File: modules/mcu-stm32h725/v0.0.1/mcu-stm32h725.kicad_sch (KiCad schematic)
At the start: 14 parts, among them J1 USB-C, U1 USB6B1RL, U2 TPS2116DRLR, U3 TLV62569DBVR

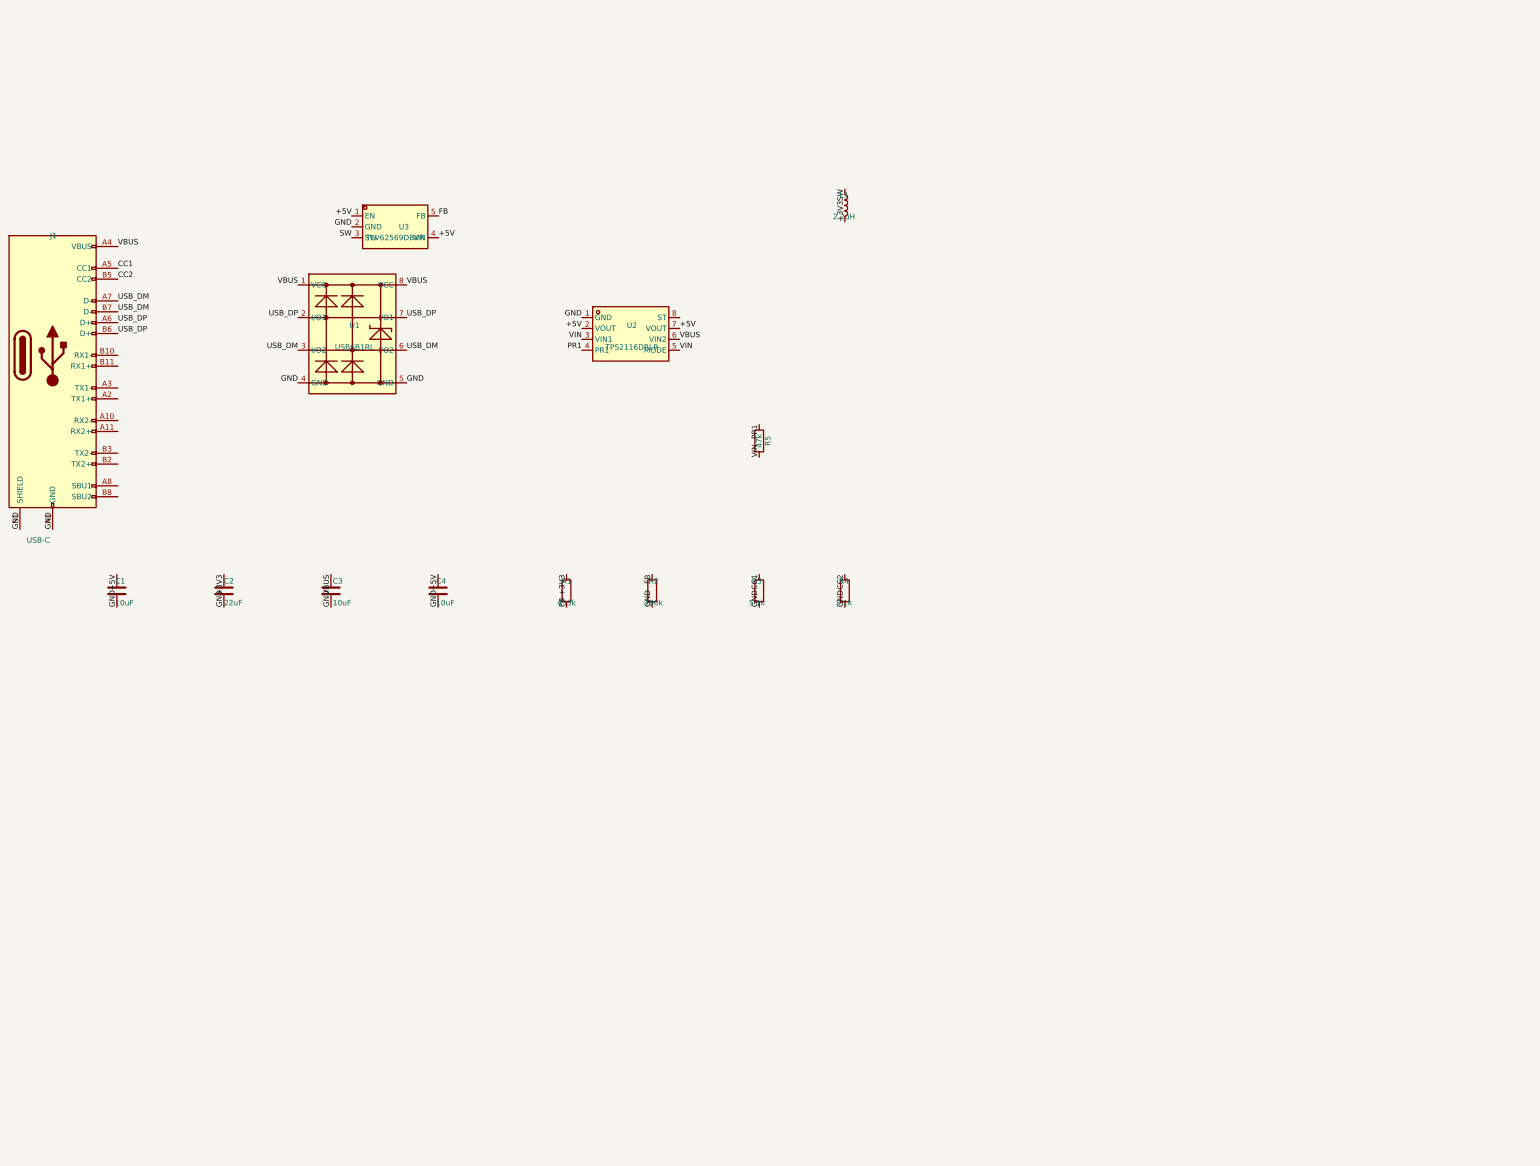
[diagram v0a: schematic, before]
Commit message: Complete mcu-stm32h725 schematic: MCU core + full GPIO breakout (ERC 0 errors)
Direct-SMPS power tree (VDDSMPS/VLXSMPS+L2/VFBSMPS=VCORE per DS13311 Table 16), full VDD/VCAP/VDDA decoupling, HSE crystal, BOOT0/NRST, USB to PA11/12. All 44 GPIO broken out by RAW pin name (no aliasing) to edge connectors J2 (Side A) + J3 (Side B). PWR_FLAGs + no-connects on unused USB-C SS/SBU + TPS2116 ST. 4-layer PCB chosen. ERC: 0 errors, 130 benign easyeda-symbol warnings.

Co-Authored-By: Claude Opus 4.8 <noreply@anthropic.com>
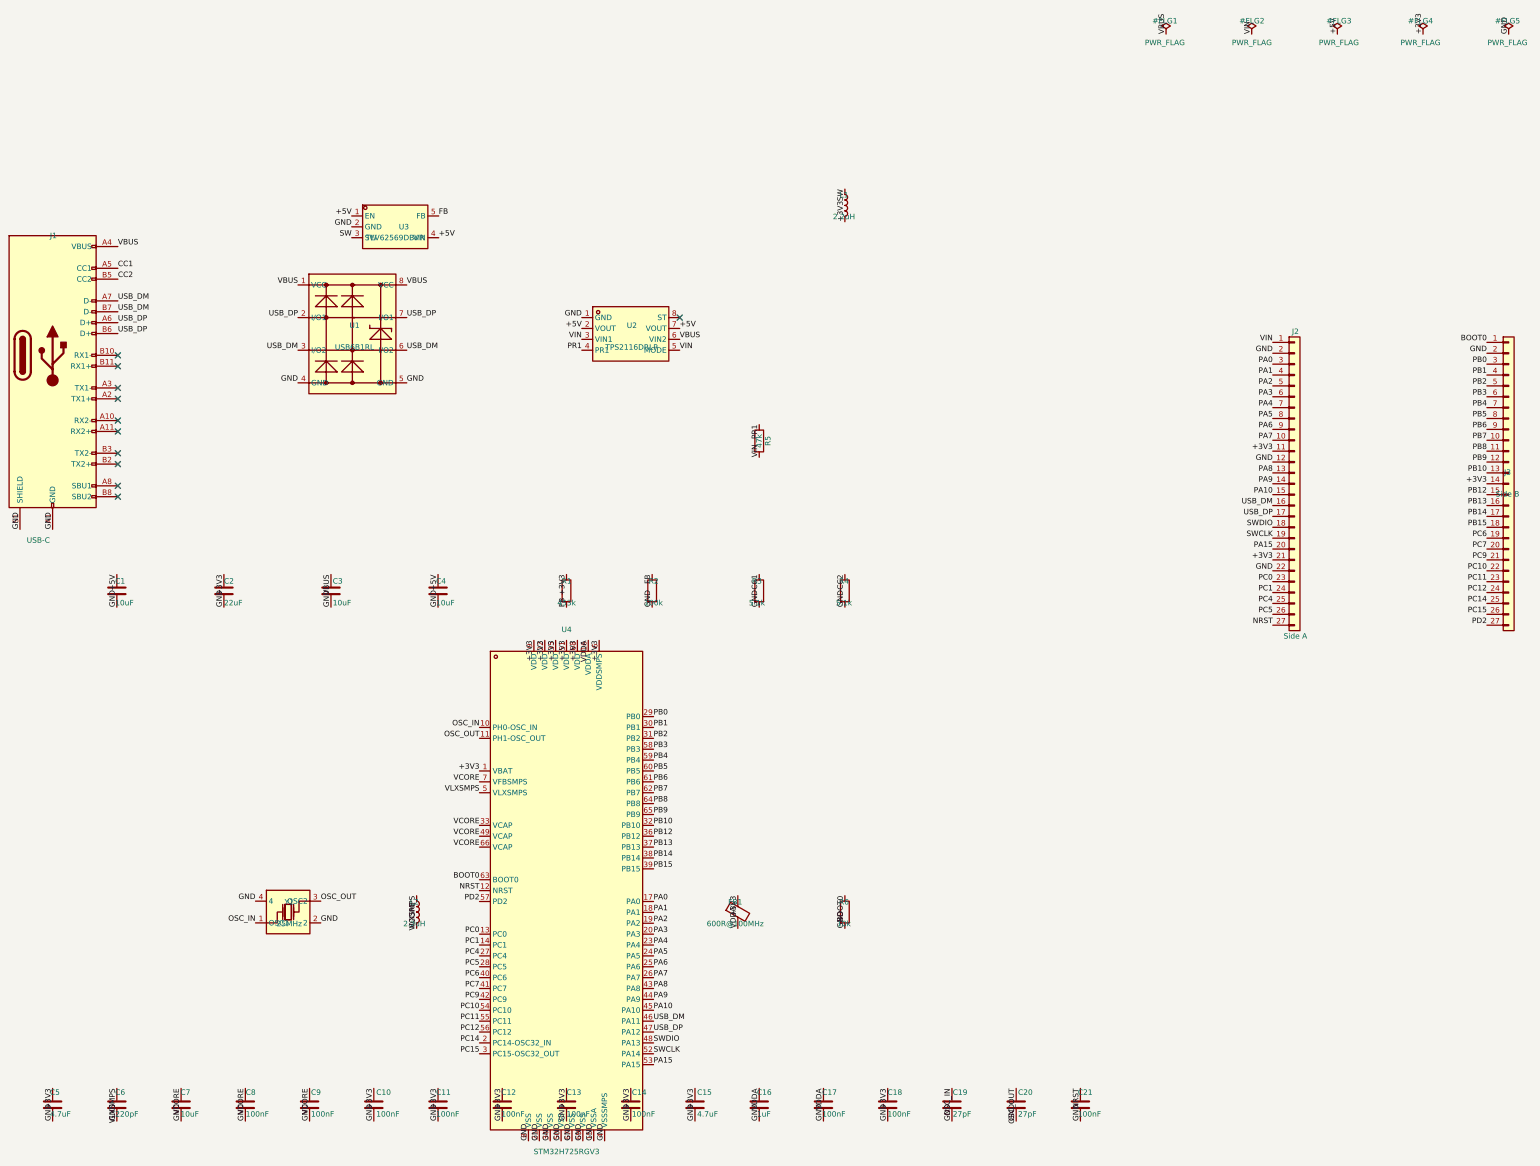
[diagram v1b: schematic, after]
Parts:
- added C10, C11, C12, C13, C14, C17, C18, C21, C8, C9: 100nF, Capacitor_SMD:C_0402_1005Metric, symbol Device:C
- added C15, C5: 4.7uF, Capacitor_SMD:C_0805_2012Metric, symbol Device:C
- added C16: 1uF, Capacitor_SMD:C_0805_2012Metric, symbol Device:C
- added C19, C20: 27pF, Capacitor_SMD:C_0402_1005Metric, symbol Device:C
- added C6: 220pF, Capacitor_SMD:C_0402_1005Metric, symbol Device:C
- added C7: 10uF, Capacitor_SMD:C_0805_2012Metric, symbol Device:C
- added FB1: 600R@100MHz, Inductor_SMD:L_0805_2012Metric, symbol Device:FerriteBead
- added J2: Side A, symbol Connector_Generic:Conn_01x27
- added J3: Side B, symbol Connector_Generic:Conn_01x27
- added L2: 2.2uH, Inductor_SMD:L_2520_2520Metric, symbol Device:L
- added R6: 10k, Resistor_SMD:R_0603_1608Metric, symbol Device:R
- added U4: STM32H725RGV3, symbol mcu-stm32h725:STM32H725RGV3
- added Y1: 25MHz, symbol mcu-stm32h725:ECS-250-20-33-DU-TR
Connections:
- net +3V3: now also C10.1, C11.1, C12.1, C13.1, C14.1, C15.1, C18.1, C5.1, FB1.1, J2.11 (Pin_11), J2.21 (Pin_21), J3.14 (Pin_14), U4.1 (VBAT), U4.22 (VDD), U4.35 (VDD), U4.51 (VDD), U4.6 (VDDSMPS), U4.68 (VDD), U4.9 (VDD)
- net GND: now also C10.2, C11.2, C12.2, C13.2, C14.2, C15.2, C16.2, C17.2, C18.2, C19.2, C20.2, C21.2, C5.2, C6.2, C7.2, C8.2, C9.2, J2.12 (Pin_12), J2.2 (Pin_2), J2.22 (Pin_22), J3.2 (Pin_2), R6.2, U4.15 (VSSA), U4.21 (VSS), U4.34 (VSS), U4.4 (VSSSMPS), U4.50 (VSS), U4.67 (VSS), U4.69 (VSS), U4.8 (VSS), Y1.2, Y1.4
- net USB_DM: now also J2.16 (Pin_16), U4.46 (PA11)
- net USB_DP: now also J2.17 (Pin_17), U4.47 (PA12)
- net VIN: now also J2.1 (Pin_1)
- new net BOOT0: J3.1 (Pin_1), R6.1, U4.63 (BOOT0)
- new net NRST: C21.1, J2.27 (Pin_27), U4.12 (NRST)
- new net OSC_IN: C19.1, U4.10 (PH0-OSC_IN), Y1.1 (OSC1)
- new net OSC_OUT: C20.1, U4.11 (PH1-OSC_OUT), Y1.3 (OSC2)
- new net PA0: J2.3 (Pin_3), U4.17 (PA0)
- new net PA1: J2.4 (Pin_4), U4.18 (PA1)
- new net PA10: J2.15 (Pin_15), U4.45 (PA10)
- new net PA15: J2.20 (Pin_20), U4.53 (PA15)
- new net PA2: J2.5 (Pin_5), U4.19 (PA2)
- new net PA3: J2.6 (Pin_6), U4.20 (PA3)
- new net PA4: J2.7 (Pin_7), U4.23 (PA4)
- new net PA5: J2.8 (Pin_8), U4.24 (PA5)
- new net PA6: J2.9 (Pin_9), U4.25 (PA6)
- new net PA7: J2.10 (Pin_10), U4.26 (PA7)
- new net PA8: J2.13 (Pin_13), U4.43 (PA8)
- new net PA9: J2.14 (Pin_14), U4.44 (PA9)
- new net PB0: J3.3 (Pin_3), U4.29 (PB0)
- new net PB1: J3.4 (Pin_4), U4.30 (PB1)
- new net PB10: J3.13 (Pin_13), U4.32 (PB10)
- new net PB12: J3.15 (Pin_15), U4.36 (PB12)
- new net PB13: J3.16 (Pin_16), U4.37 (PB13)
- new net PB14: J3.17 (Pin_17), U4.38 (PB14)
- new net PB15: J3.18 (Pin_18), U4.39 (PB15)
- new net PB2: J3.5 (Pin_5), U4.31 (PB2)
- new net PB3: J3.6 (Pin_6), U4.58 (PB3)
- new net PB4: J3.7 (Pin_7), U4.59 (PB4)
- new net PB5: J3.8 (Pin_8), U4.60 (PB5)
- new net PB6: J3.9 (Pin_9), U4.61 (PB6)
- new net PB7: J3.10 (Pin_10), U4.62 (PB7)
- new net PB8: J3.11 (Pin_11), U4.64 (PB8)
- new net PB9: J3.12 (Pin_12), U4.65 (PB9)
- new net PC0: J2.23 (Pin_23), U4.13 (PC0)
- new net PC1: J2.24 (Pin_24), U4.14 (PC1)
- new net PC10: J3.22 (Pin_22), U4.54 (PC10)
- new net PC11: J3.23 (Pin_23), U4.55 (PC11)
- new net PC12: J3.24 (Pin_24), U4.56 (PC12)
- new net PC14: J3.25 (Pin_25), U4.2 (PC14-OSC32_IN)
- new net PC15: J3.26 (Pin_26), U4.3 (PC15-OSC32_OUT)
- new net PC4: J2.25 (Pin_25), U4.27 (PC4)
- new net PC5: J2.26 (Pin_26), U4.28 (PC5)
- new net PC6: J3.19 (Pin_19), U4.40 (PC6)
- new net PC7: J3.20 (Pin_20), U4.41 (PC7)
- new net PC9: J3.21 (Pin_21), U4.42 (PC9)
- new net PD2: J3.27 (Pin_27), U4.57 (PD2)
- new net SWCLK: J2.19 (Pin_19), U4.52 (PA14)
- new net SWDIO: J2.18 (Pin_18), U4.48 (PA13)
- new net VCORE: C7.1, C8.1, C9.1, L2.2, U4.33 (VCAP), U4.49 (VCAP), U4.66 (VCAP), U4.7 (VFBSMPS)
- new net VDDA: C16.1, C17.1, FB1.2, U4.16 (VDDA)
- new net VLXSMPS: C6.1, L2.1, U4.5 (VLXSMPS)
- no-connect marks 0 -> 11

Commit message: Add PCB: 4-layer outline (68.6x18mm) + castellated edges for mcu-stm32h725
F8-imported netlist (37 footprints, 62 nets verified). Board outline drawn to size on Edge.Cuts; J2/J3 castellation strips (27 plated half-holes @ 2.54mm) on the long edges, pads bisected by the cut. Custom Castellation_1x27_P2.54mm_Edge footprint. Edited .kicad_pcb directly (MCP board write/save broken in this env). NOTE: board refs re-annotated by F8 (!= schematic) - reconcile via back-annotation before deliverables.

Co-Authored-By: Claude Opus 4.8 <noreply@anthropic.com>
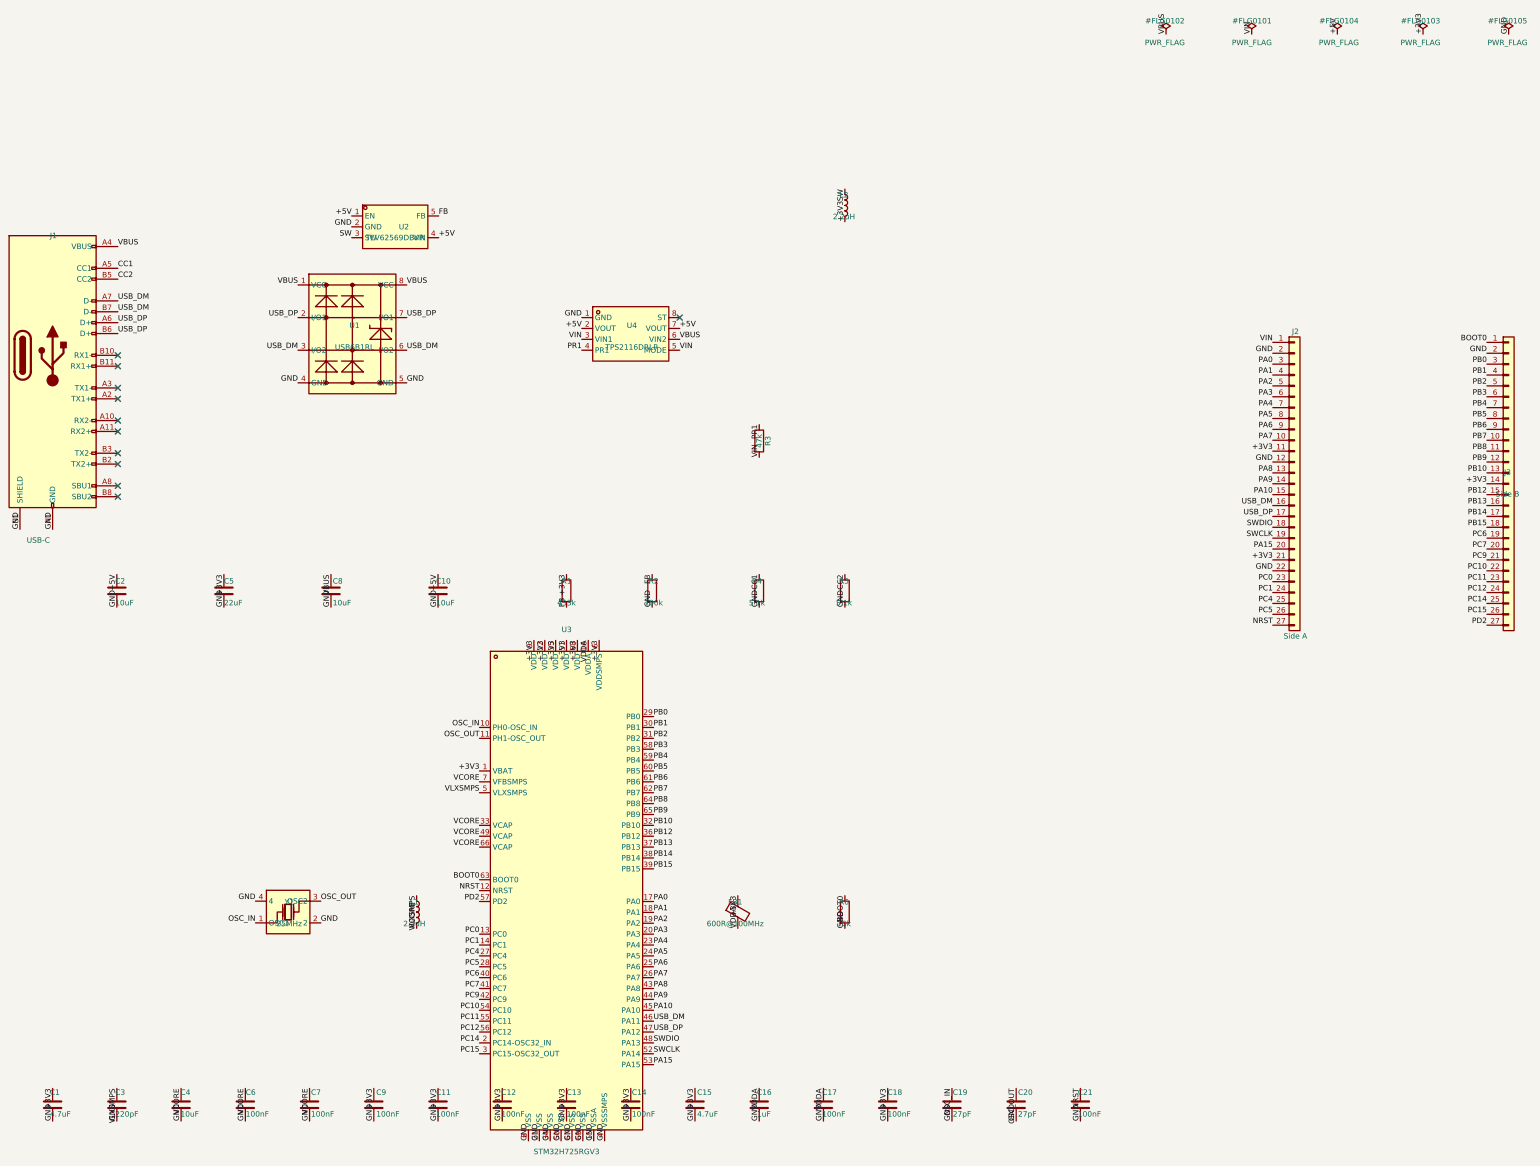
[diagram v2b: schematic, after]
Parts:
- J2, J3: footprint (none) -> mcu-stm32h725:Castellation_1x27_P2.54mm_Edge
- U3: renamed from U4; footprint (none) -> mcu-stm32h725:QFN-68_L8.0-W8.0-P0.40-BL-EP6.4
- Y1: footprint (none) -> mcu-stm32h725:CRYSTAL-SMD_4P-L3.2-W2.5-BL
- renumbered C5 to C1, C4 to C10, C1 to C2, C6 to C3, C7 to C4, C2 to C5, C8 to C6, C9 to C7, C3 to C8, C10 to C9, L2 to L1, L1 to L2, R5 to R3, R3 to R4, R4 to R5, U3 to U2, U2 to U4
